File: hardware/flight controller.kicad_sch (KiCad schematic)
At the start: 88 parts, among them J1 Input Power, J10 M9, J11 M10, J12 M11, J13 M12, J14 Video In, J15 LED Strip, J16 Video Out, J17 I2C4, J18 UART2, J19 UART7, J2 M1, J20 SWD, J21 UART5, J22 UART8, J23 UART3, J24 UART4, J25 USB_C_Receptacle_USB2.0_16P, J26 Micro_SD_Card, J27 GPIO, J3 M2, J4 M3, J5 M4, J6 M5, J7 M6, J8 M7, J9 M8, U1 AP2114HA-3.3TRG1, U2 BMP388, U3 LIS3MDLTR, U4 STM32H743VITx, U5 AT7456E, U6 ICM-42688-P, Y1 27MHz, Y2 16MHz, Y3 32.768kHz

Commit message: finished bom
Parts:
- removed C14, C15: 100nF, Capacitor_SMD:C_0805_2012Metric, symbol Device:C
- removed U1: AP2114HA-3.3TRG1, Package_TO_SOT_SMD:SOT-223, symbol lcsc:AP2114HA-3.3TRG1
- removed U3: LIS3MDLTR, Package_LGA:LGA-12_2x2mm_P0.5mm, symbol lcsc:LIS3MDLTR
- added C16: 100nF, Capacitor_SMD:C_0805_2012Metric, symbol Device:C
- added C17: 4.7uF, Capacitor_SMD:C_0805_2012Metric, symbol Device:C
- added C3: 47pF, Capacitor_SMD:C_0805_2012Metric, symbol Device:C
- added C4, C5: 22uF, Capacitor_SMD:C_1206_3216Metric, symbol Device:C
- added L1: 6.8uH, Inductor_SMD:L_APV_APH0630, symbol Device:L
- added R2: 100K, Resistor_SMD:R_0805_2012Metric, symbol Device:R
- added R8: 22K, Resistor_SMD:R_0805_2012Metric, symbol Device:R
- added U1: TPS54302, Package_TO_SOT_SMD:SOT-23-6, symbol Regulator_Switching:TPS54302
- added U3: QMC5883P, Package_LGA:LGA-16_3x3mm_P0.5mm, symbol lcsc:QMC5883P
- C1: value 4.7uF -> 100nF
- C2: value 4.7uF -> 10uF
- R10: renamed from R8; value 4.7K -> 3.3K
- R19: value 56 -> 75
- R3: renamed from R2; value 4.7K -> 3.3K
- R5: renamed from R4; value 4.7K -> 3.3K
- R7: renamed from R6; value 4.7K -> 3.3K
- renumbered C9 to C10, C13 to C11, C7 to C12, C8 to C13, C10 to C14, C11 to C15, C16 to C18, C17 to C19, C18 to C20, C19 to C21, C12 to C22, C20 to C23, C21 to C24, C22 to C25, C24 to C26, C23 to C28, C26 to C29, C25 to C30, C3 to C6, C4 to C7, C5 to C8, C6 to C9, D5 to D1, D1 to D2, D2 to D3, D3 to D4, D4 to D5, J9 to J10, J10 to J11, J11 to J12, J12 to J13, J13 to J14, J17 to J15, J14 to J16, J16 to J17, J15 to J18, J25 to J19, J18 to J20, J19 to J21, J21 to J22, J22 to J23, J27 to J24, J20 to J25, J23 to J26, J24 to J27, J26 to J8, J8 to J9, R9 to R11, R10 to R12, R12 to R13, R13 to R14, R11 to R16, R14 to R17, R16 to R18, R17 to R20, R18 to R21, R3 to R4, R5 to R6, R7 to R9
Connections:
- net +3.3V: now also C16.1, C3.1, C4.2, C5.1, L1.2, R2.1, U3.2 (VDD); no longer C2.1
- net +5V: now also C2.1, U1.3 (VIN); no longer C1.1
- net GND: now also C16.2, C17.2, C4.1, C5.2, R8.2, U1.1 (GND), U3.11 (GND), U3.9 (GND); no longer C1.2
- net I2C_SCL: now also U3.1 (SCK)
- net I2C_SDA: now also U3.16 (SDA)
- new net: C3.2, R2.2, R8.1, U1.4 (FB)
- new net: C1.1, L1.1, U1.2 (SW)
- new net: C1.2, U1.6 (BOOT)
- new net: C17.1, U3.10 (C1)
- no-connect marks 20 -> 18
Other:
- moved on the sheet: C12, C13, U2

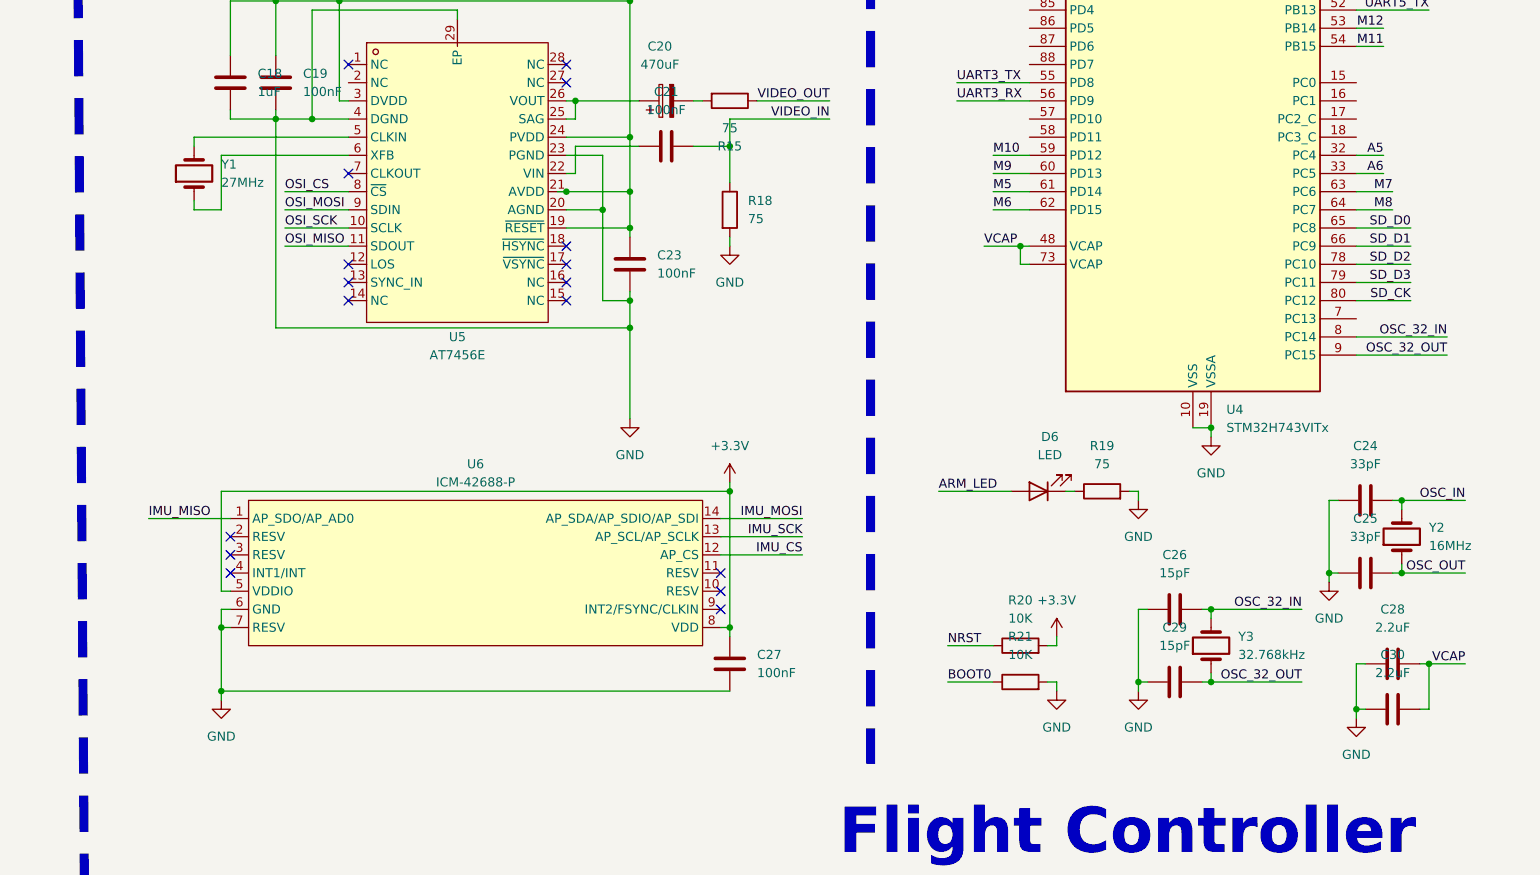
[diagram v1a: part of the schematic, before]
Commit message: smd crystal
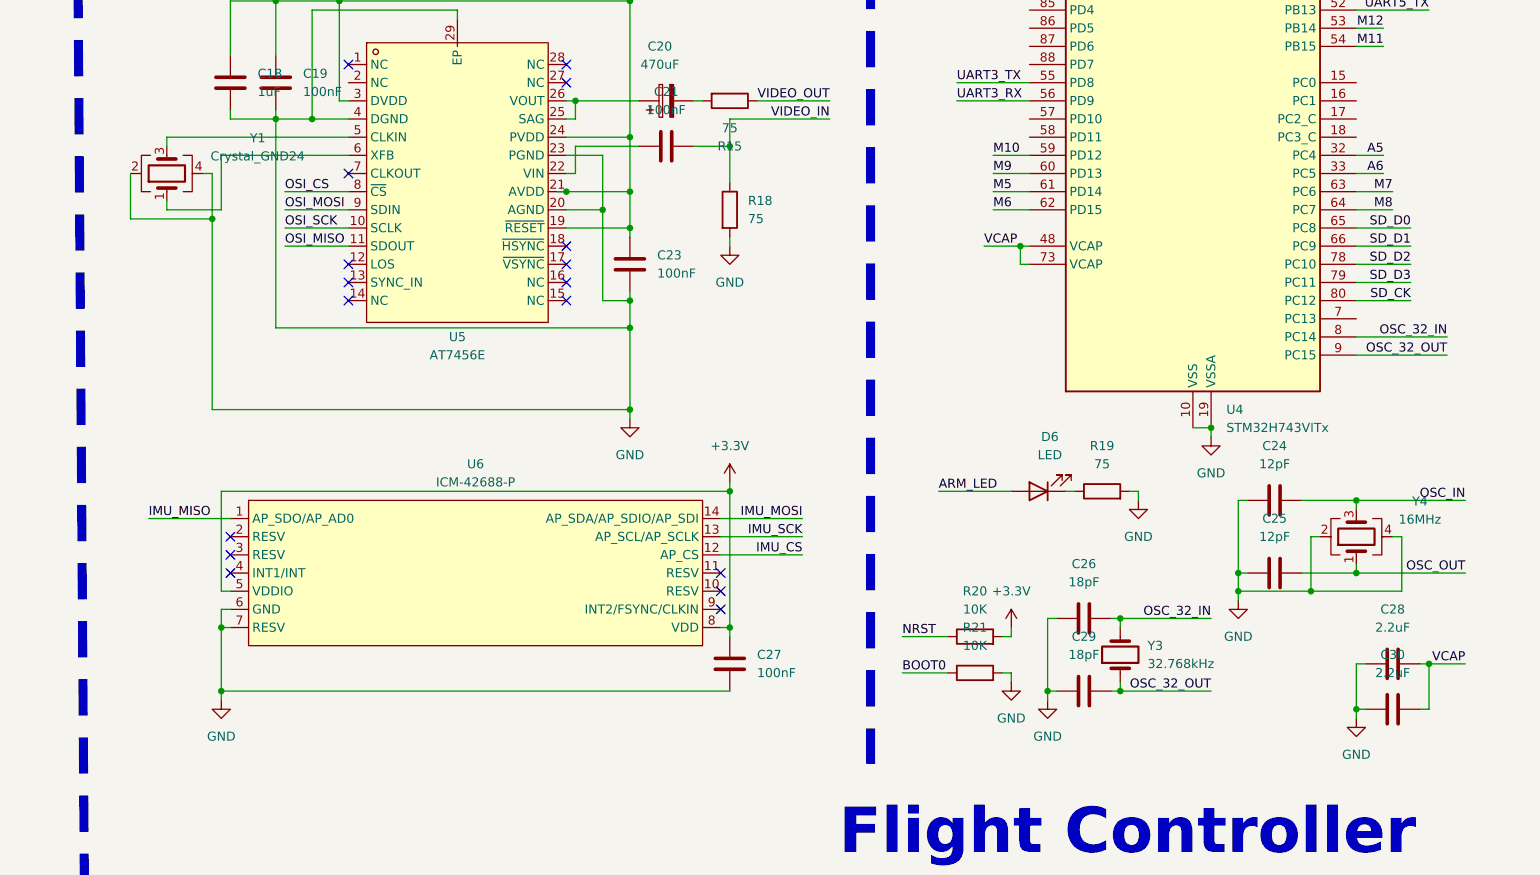
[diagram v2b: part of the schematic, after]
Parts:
- removed Y1: 27MHz, Crystal:Crystal_HC49-U_Vertical, symbol Device:Crystal
- removed Y2: 16MHz, Crystal:Crystal_HC49-U_Vertical, symbol Device:Crystal
- added Y1: Crystal_GND24, Crystal:Crystal_SMD_3225-4Pin_3.2x2.5mm, symbol Device:Crystal_GND24
- added Y4: 16MHz, Crystal:Crystal_SMD_3225-4Pin_3.2x2.5mm, symbol Device:Crystal_GND24
- C24, C25: value 33pF -> 12pF
- C26, C29: value 15pF -> 18pF
- Y3: footprint Crystal:Crystal_DS26_D2.0mm_L6.0mm_Horizontal -> Crystal:Crystal_SMD_3215-2Pin_3.2x1.5mm
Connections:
- net GND: now also Y1.2, Y1.4, Y4.2, Y4.4
- net OSC_IN: now also Y4.3
- net OSC_OUT: now also Y4.1
- net at U5.5 (CLKIN): now also Y1.3
- net at U5.6 (XFB): now also Y1.1
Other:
- moved on the sheet: C24, C25, C26, C29, R20, R21, Y3

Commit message: smol
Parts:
- removed C12, C19, C21, C23: 100nF, Capacitor_SMD:C_0805_2012Metric, symbol Device:C
- removed C18: 1uF, Capacitor_SMD:C_0805_2012Metric, symbol Device:C
- removed C20: 470uF, Capacitor_THT:CP_Radial_D8.0mm_P3.50mm, symbol Device:C_Polarized
- removed C22: 1000uF, Capacitor_THT:CP_Radial_D8.0mm_P3.50mm, symbol Device:C_Polarized
- removed R15, R18: 75, Resistor_SMD:R_0805_2012Metric, symbol Device:R
- removed U5: AT7456E, Package_SO:TSSOP-28-1EP_4.4x9.7mm_P0.65mm_EP2.85x6.7mm, symbol lcsc:AT7456E
- removed Y1: Crystal_GND24, Crystal:Crystal_SMD_3225-4Pin_3.2x2.5mm, symbol Device:Crystal_GND24
- added C31, C32: 22uF, Capacitor_SMD:C_1206_3216Metric, symbol Device:C
- added C33, C34: 100nF, Capacitor_SMD:C_0603_1608Metric, symbol Device:C
- added C35: 1uF, Capacitor_SMD:C_0603_1608Metric, symbol Device:C
- added R22: 1K, Resistor_SMD:R_0603_1608Metric, symbol Device:R
- added R23, R24: 75, Resistor_SMD:R_0603_1608Metric, symbol Device:R
- added U7: AT7456ELAH_C42388749, lcsc:LGA-16_L6.8-W4.0-P0.65-TL-2EP, symbol lcsc:AT7456ELAH_C42388749
- added Y2: Crystal_GND24, Crystal:Crystal_SMD_3225-4Pin_3.2x2.5mm, symbol Device:Crystal_GND24
- C1, C10, C11, C13, C14, C15, C16, C24, C25, C26, C27, C28, C29, C3, C30, C6, C7, C8, C9: footprint Capacitor_SMD:C_0805_2012Metric -> Capacitor_SMD:C_0603_1608Metric
- D1: value 1N4001 -> SS54; footprint Diode_THT:D_DO-41_SOD81_P7.62mm_Horizontal -> Diode_SMD:D_SMA
- R1, R10, R11, R12, R13, R14, R16, R17, R19, R2, R20, R21, R3, R4, R5, R6, R7, R8, R9: footprint Resistor_SMD:R_0805_2012Metric -> Resistor_SMD:R_0603_1608Metric
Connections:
- net +3.3V: now also C33.1, C34.1, C35.1, R22.2, U7.12 (AVDD), U7.14 (PVDD), U7.2 (DVDD)
- net GND: now also C33.2, C34.2, C35.2, R24.1, U7.1 (DGND), U7.10 (AGND), U7.11 (PGND), U7.17 (EP1), U7.18 (EP2), Y2.2, Y2.4
- net OSI_CS: now also U7.5 (~{CS})
- net OSI_MISO: now also U7.8 (SDOUT)
- net OSI_MOSI: now also U7.6 (SDIN)
- net OSI_SCK: now also U7.7 (SCLK)
- net VIDEO_IN: now also R24.2, U7.13 (VIN)
- net VIDEO_OUT: now also R23.2
- new net: C31.1, U7.16 (VOUT)
- new net: C31.2, C32.2, R23.1
- new net: C32.1, U7.15 (SAG)
- new net: U7.3 (CLKIN), Y2.3
- new net: U7.4 (XFB), Y2.1
- new net: R22.1, U7.9 (~{RESET})
- no-connect marks 18 -> 7
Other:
- moved on the sheet: C16, C17, U3

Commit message: idk
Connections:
- net A1: now also U4.31 (PA7); no longer U4.28 (PA4)
- net A2: now also U4.33 (PC5); no longer U4.29 (PA5)
- net A3: now also U4.35 (PB1); no longer U4.30 (PA6)
- net A4: now also U4.34 (PB0); no longer U4.31 (PA7)
- net A6: now also U4.30 (PA6); no longer U4.33 (PC5)
- net A7: now also U4.29 (PA5); no longer U4.34 (PB0)
- net A8: now also U4.28 (PA4); no longer U4.35 (PB1)
- net M1: now also U4.61 (PD14); no longer U4.43 (PE13)
- net M10: now also U4.46 (PB10)
- net M11: now also U4.64 (PC7)
- net M12: now also U4.47 (PB11)
- net M2: no longer U4.44 (PE14)
- net M3: no longer U4.46 (PB10)
- net M4: now also U4.43 (PE13); no longer U4.47 (PB11)
- net M5: now also U4.62 (PD15); no longer U4.61 (PD14)
- net M6: no longer U4.62 (PD15)
- net M7: no longer U4.63 (PC6)
- net M8: now also U4.44 (PE14); no longer U4.64 (PC7)
- net M9: now also U4.63 (PC6)
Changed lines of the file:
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@@
 		)
 	)
-	(label "M5"
+	(label "M1"
 		(at 337.82 172.72 0)
 		(effects
@@
 		)
 	)
-	(label "M7"
+	(label "M9"
 		(at 393.7 172.72 180)
 		(effects
@@
 		)
 	)
-	(label "M6"
+	(label "M5"
 		(at 337.82 175.26 0)
 		(effects
@@
 		)
 	)
-	(label "M1"
+	(label "M4"
 		(at 339.09 127 0)
 		(effects
@@
 		)
 	)
-	(label "A4"
+	(label "A1"
 		(at 392.43 88.9 180)
 		(effects
@@
 		)
 	)
-	(label "A2"
+	(label "A7"
 		(at 392.43 83.82 180)
 		(effects
@@
 		)
 	)
-	(label "A8"
+	(label "A3"
 		(at 392.43 116.84 180)
 		(effects
@@
 		)
 	)
-	(label "A7"
+	(label "A4"
 		(at 392.43 114.3 180)
 		(effects
@@
 		)
 	)
-	(label "M4"
+	(label "M12"
 		(at 392.43 142.24 180)
 		(effects
@@
 		)
 	)
-	(label "A1"
+	(label "A8"
 		(at 392.43 81.28 180)
 		(effects
@@
 		)
 	)
-	(label "M3"
+	(label "M10"
 		(at 392.43 139.7 180)
 		(effects
@@
 		)
 	)
-	(label "A6"
+	(label "A2"
 		(at 392.43 170.18 180)
 		(effects
@@
 		)
 	)
-	(label "A3"
+	(label "A6"
 		(at 392.43 86.36 180)
 		(effects
@@
 		)
 	)
-	(label "M8"
+	(label "M11"
 		(at 393.7 175.26 180)
 		(effects
@@
 		)
 	)
-	(label "M2"
+	(label "M8"
 		(at 339.09 129.54 0)
 		(effects

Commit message: some routing
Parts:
- J21: value UART7 -> UART3
- J26: value UART3 -> UART6
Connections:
- net M1: now also U4.53 (PB14); no longer U4.61 (PD14)
- net M10: now also U4.24 (PA2); no longer U4.46 (PB10), U4.59 (PD12)
- net M11: now also U4.46 (PB10); no longer U4.54 (PB15), U4.64 (PC7)
- net M12: now also U4.25 (PA3); no longer U4.47 (PB11), U4.53 (PB14)
- net M2: now also U4.43 (PE13)
- net M3: now also U4.39 (PE9)
- net M4: now also U4.22 (PA0); no longer U4.43 (PE13)
- net M5: now also U4.54 (PB15); no longer U4.62 (PD15)
- net M6: now also U4.44 (PE14)
- net M7: now also U4.41 (PE11)
- net M8: now also U4.23 (PA1); no longer U4.44 (PE14)
- net M9: now also U4.47 (PB11); no longer U4.60 (PD13), U4.63 (PC6)
- net UART2_CTS: no longer U4.22 (PA0)
- net UART2_RTS: no longer U4.23 (PA1)
- net UART2_RX: no longer U4.25 (PA3)
- net UART2_TX: no longer U4.24 (PA2)
- net UART3_RX: now also J21.2 (Pin_2); no longer J26.2 (Pin_2)
- net UART3_TX: now also J21.1 (Pin_1); no longer J26.1 (Pin_1)
- net UART3_CTS: now reaches U4.58 (PD11)
- net UART3_CTS: now also J21.3 (Pin_3)
- net UART7_CTS: no longer names the net of U4.40 (PE10)
- net UART7_CTS: no longer J21.3 (Pin_3)
- net UART7_RTS renamed UART3_RTS
- net UART3_RTS: now also U4.59 (PD12); no longer U4.39 (PE9)
- net UART7_RX: no longer names the net of U4.37 (PE7)
- net UART7_RX: no longer J21.2 (Pin_2)
- net UART7_TX: no longer names the net of U4.38 (PE8)
- net UART7_TX: no longer J21.1 (Pin_1)
- new net UART6_RX: J26.2 (Pin_2), U4.64 (PC7)
- new net UART6_TX: J26.1 (Pin_1), U4.63 (PC6)

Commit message: finish v2
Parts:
- removed D3, D4, D5: WS2812B, LED_SMD:LED_WS2812B_PLCC4_5.0x5.0mm_P3.2mm, symbol LED:WS2812B
- Y1: renamed from Y2; value Crystal_GND24 -> 27MHz
- renumbered C13 to C12, C16 to C13, C17 to C16, C35 to C17, C34 to C18, C31 to C19, C32 to C20, C33 to C21, C24 to C22, C25 to C23, C26 to C24, C27 to C25, C28 to C26, C29 to C27, C30 to C28, D6 to D3, R23 to R14, R14 to R15, R24 to R16, R22 to R17, R16 to R18, R17 to R19, R19 to R20, R20 to R21, R21 to R22, U7 to U5, Y4 to Y2
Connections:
- net ARM_LED: now also U4.7 (PC13); no longer U4.2 (PE3)
- net M10: now also U4.23 (PA1); no longer U4.24 (PA2)
- net M12: now also U4.22 (PA0); no longer U4.25 (PA3)
- net M4: now also U4.25 (PA3); no longer U4.22 (PA0)
- net M8: now also U4.24 (PA2); no longer U4.23 (PA1)
- net UART2_CTS: now also U4.84 (PD3)
- net UART2_RTS: now also U4.85 (PD4)
- net UART2_RX: now also U4.87 (PD6)
- net UART2_TX: now also U4.86 (PD5)
- net at J18.1 (Pin_1): now also D2.2 (DOUT)
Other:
- moved on the sheet: J18
